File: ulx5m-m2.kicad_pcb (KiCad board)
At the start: 6 copper layers, 22 x 60 mm, 234 parts, among them J101 JTAG_EXT, J102 3V3_PSU, J3 Vcore_sel, J4 JTAG, J5 USB_C_Receptacle, SW1 219-2MST, U1 TLV62569DBV, U10 IS42S16320D-6BLI, U3 MPM3833CGRH-Z, U4 GateMate-CCGM1A1, U5 TLV62569DBV, U6 74LVC1G04GM,115, U7 74LVC2G00HK3-7, U8 74LVC2G00HK3-7, U9 AT25QL321-MBUE-T, X2 511FCA100M000BAG, Y1 ASE2-25.000MHZ-L-C-T

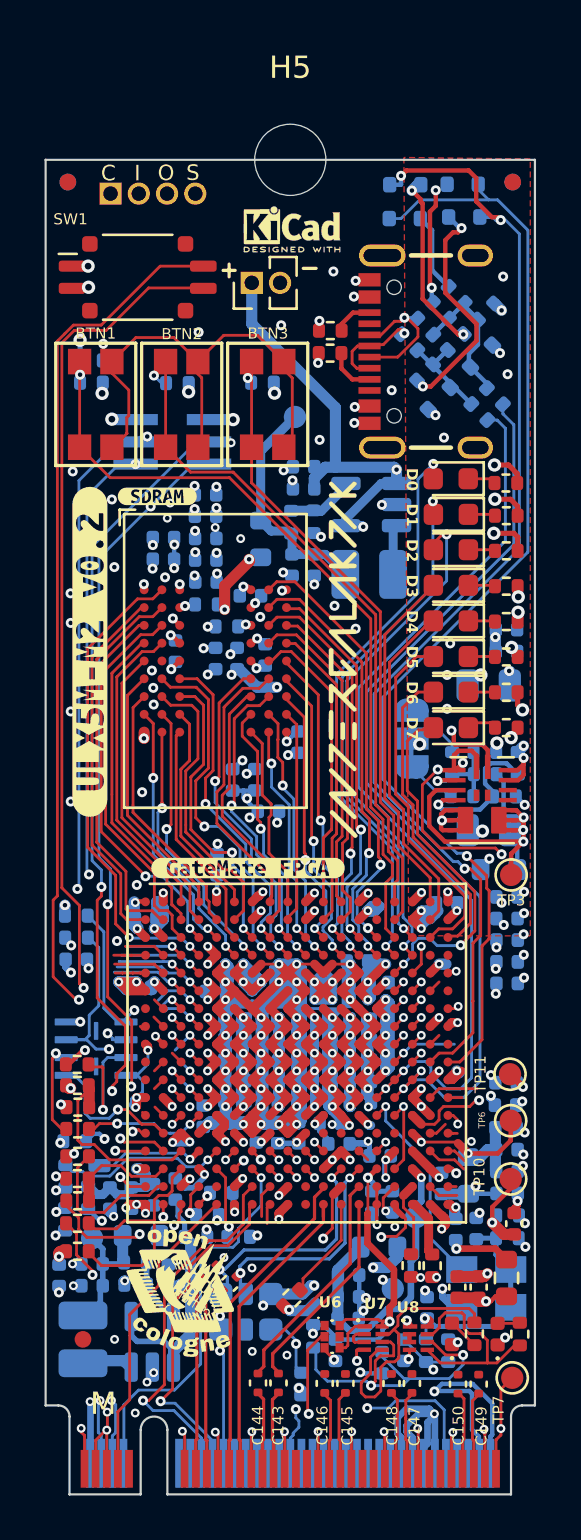
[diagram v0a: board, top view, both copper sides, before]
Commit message: update to JLCPCB capabilities
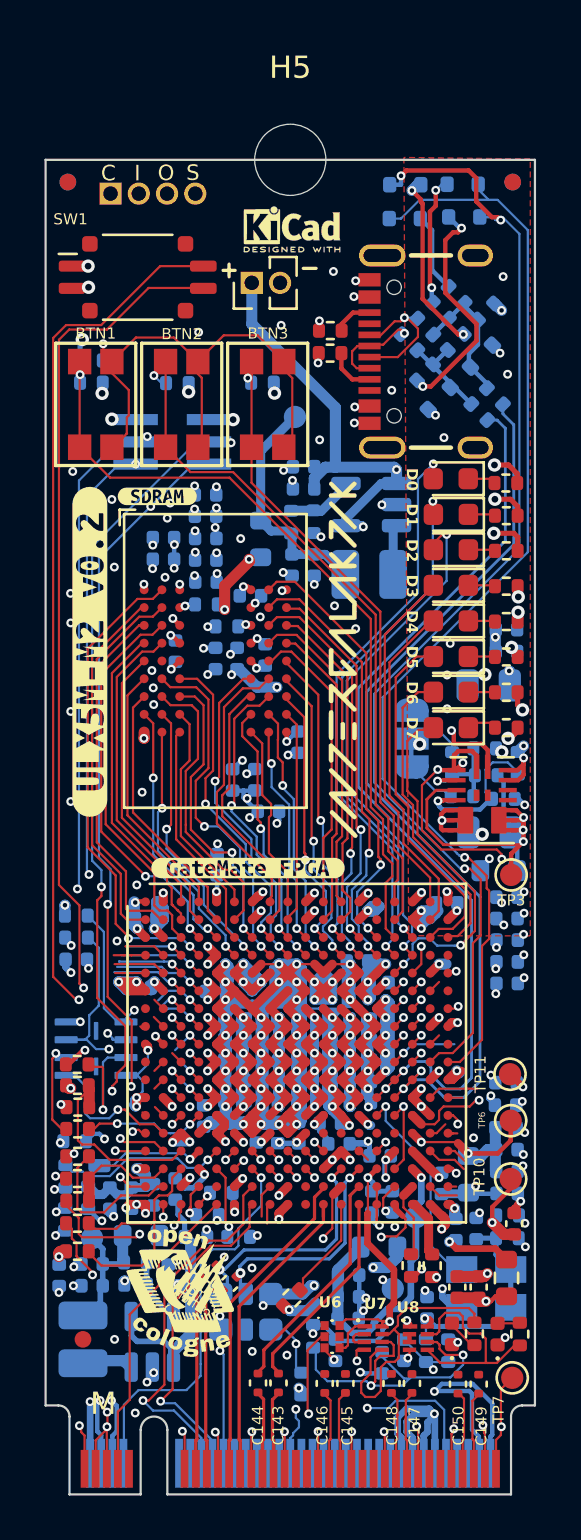
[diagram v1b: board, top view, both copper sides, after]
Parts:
- moved R12 0.16 mm to (67.0, 100.5)
- moved R2 0.12 mm to (67.9, 102.8)
- moved C10 0.10 mm to (67.3, 104.3)
- moved R15 0.07 mm to (67.1, 101.8)
- moved R13 0.05 mm to (67.7, 106.0)
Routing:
- net GND: track 822.3 -> 823.9 mm, vias 226 -> 225
- net Net-(D6-A): track 5.21 -> 5.83 mm
